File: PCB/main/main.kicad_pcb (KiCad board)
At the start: 2 copper layers, 4 parts, among them J1 Conn_01x33_Female, J2 Conn_01x33_Female, J3 Conn_01x33_Female, J4 Conn_01x33_Female

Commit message: Updated kicad_pcb file
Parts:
- added BT1: Battery, EEE3088F_Footprints:18650_Holder_THT, F.Cu at (228.6, 76.2)
- added C1: 22u, EEE3088F_Footprints:CAPC3216X180N, F.Cu at (278.9, 69.7)
- added C10: 100nF, EEE3088F_Footprints:CAPC1005X55N, F.Cu at (228.9, 109.6)
- added C11: 1.0uF, EEE3088F_Footprints:CAPC1608X90N, F.Cu at (199.6, 119.4)
- added C12: 0.1uF, EEE3088F_Footprints:CAPC1005X55N, F.Cu at (202.8, 119.2)
- added C13: 0.1uF, EEE3088F_Footprints:CAPC1005X55N, F.Cu at (213.7, 108.3)
- added C2: 10u, EEE3088F_Footprints:CAPC3216X180N, F.Cu at (270.4, 80.0)
- added C3: 22u, EEE3088F_Footprints:CAPC3216X180N, F.Cu at (222.6, 88.8)
- added C4: 10u, EEE3088F_Footprints:CAPC3216X180N, F.Cu at (203.0, 98.8)
- added C5: 0.47u, EEE3088F_Footprints:CAPC1005X55N, F.Cu at (220.2, 96.1)
- added C6: 1u, EEE3088F_Footprints:CAPC1608X90N, F.Cu at (231.0, 88.4)
- added C7: 10u, EEE3088F_Footprints:CAPC3216X180N, F.Cu at (217.4, 93.5)
- added C8: 22u, EEE3088F_Footprints:CAPC3216X180N, F.Cu at (208.2, 98.8)
- added C9: 1uF, EEE3088F_Footprints:RESC1608X55N, F.Cu at (223.3, 110.9)
- added D1: GREEN, EEE3088F_Footprints:LEDC1608X50N, F.Cu at (222.1, 93.4)
- added D2: RED, EEE3088F_Footprints:LED0805-RD_RED, F.Cu at (197.8, 98.8)
- added D3: B5819W SL, EEE3088F_Footprints:SOD-123_L2.7-W1.6-LS3.7-RD-1, F.Cu at (279.2, 66.6)
- added D4: ZMMxx, EEE3088F_Footprints:LL-34_L3.5-W1.5-RD, F.Cu at (200.6, 113.9)
- added D5: ZMMxx, EEE3088F_Footprints:LL-34_L3.5-W1.5-RD, F.Cu at (200.6, 116.8)
- added D6: ZMMxx, EEE3088F_Footprints:LL-34_L3.5-W1.5-RD, F.Cu at (210.6, 105.8)
- added D7: GREEN, EEE3088F_Footprints:LEDC1608X50N, F.Cu at (215.6, 105.9)
- added D8: GREEN, EEE3088F_Footprints:LEDC1608X50N, F.Cu at (210.1, 108.7)
- added IC1: LM358DR2G, EEE3088F_Footprints:SOIC127P600X175-8N, F.Cu at (203.2, 90.6)
- added IC2: ap2007, EEE3088F_Footprints:SOIC127P600X175-9N, F.Cu at (272.1, 68.5)
- added IC3: TP4056-42-ESOP8, EEE3088F_Footprints:SOIC127P600X175-9N, F.Cu at (272.1, 75.1)
- added IC4: LM3940IMP-3.3_NOPB, EEE3088F_Footprints:SOT230P700X180-4N, F.Cu at (194.1, 91.4)
- added IC5: CP2102-GMR, EEE3088F_Footprints:QFN50P500X500X100-29N-D, F.Cu at (204.2, 108.1)
- added J5: USB_B_Micro, EEE3088F_Footprints:MICROXNJ, F.Cu at (194.9, 105.5)
- added L1: MWSA0402S-3R3MT, EEE3088F_Footprints:INDPM4442X200N, F.Cu at (211.1, 90.3)
- added Q1: AO3401A, EEE3088F_Footprints:SOT95P280X125-3N, F.Cu at (217.4, 89.6)
- added R1: 1K2, EEE3088F_Footprints:RESC1608X55N, F.Cu at (191.4, 100.1)
- added R10: 120R, EEE3088F_Footprints:R0603, F.Cu at (216.8, 98.9)
- added R11: 1K2, EEE3088F_Footprints:RESC1608X55N, F.Cu at (205.4, 116.1)
- added R12: 4.7k, EEE3088F_Footprints:RESC2013X65N, F.Cu at (205.6, 113.3)
- added R13: 1K2, EEE3088F_Footprints:RESC1608X55N, F.Cu at (209.9, 111.4)
- added R2: 1K2, EEE3088F_Footprints:RESC1608X55N, F.Cu at (227.2, 88.5)
- added R3: 1R, EEE3088F_Footprints:R1206, F.Cu at (201.8, 95.5)
- added R4: 1R, EEE3088F_Footprints:R1206, F.Cu at (192.2, 97.2)
- added R5: 100K, EEE3088F_Footprints:RESC3116X65N, F.Cu at (207.5, 95.5)
- added R6: 33K, EEE3088F_Footprints:RESC2013X65N, F.Cu at (212.4, 94.8)
- added R7: 1K2, EEE3088F_Footprints:RESC1608X55N, F.Cu at (216.7, 96.4)
- added R8: 1K8, EEE3088F_Footprints:RESC1608X55N, F.Cu at (212.8, 98.9)
- added R9: 1K8, EEE3088F_Footprints:RESC1608X55N, F.Cu at (278.4, 72.5)
- added U1: LM61BIZ/NOPD_TempSensor(TO-92), EEE3088F_Footprints:TO-92-3_L4.9-W3.7-P1.27-L, F.Cu at (224.4, 107.5)
- added U2: LPS22HBTR_Barometer, EEE3088F_Footprints:QFN50P210X200X80-10N, F.Cu at (229.7, 106.5)
- added U3: CAT24C256, EEE3088F_Footprints:SOIC127P600X175-8N, F.Cu at (193.6, 115.8)
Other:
- board outline added: 66.7 x 19.6 mm

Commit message: Began PCB layout
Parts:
- C1, C2, C3, C4, C5, C6, C7, C8, D1, D2, D3, IC1, IC2, IC3, IC4, L1, Q1, R1, R10, R2, R3, R4, R5, R6, R7, R8, R9: moved to B.Cu
- moved IC3 163.4 mm to (111.0, 48.0), turned to -90 degrees
- moved R7 119.6 mm to (110.2, 41.8), turned to 90 degrees
- moved BT1 92.0 mm to (141.0, 48.0)
- moved C1 76.4 mm to (205.7, 48.0), turned to 180 degrees
- moved D3 76.2 mm to (206.7, 43.0), turned to 180 degrees
- moved R9 75.8 mm to (202.7, 68.0), turned to 180 degrees
- moved R1 65.6 mm to (242.5, 59.0), turned to 180 degrees
- moved IC4 58.7 mm to (237.7, 52.0), turned to 180 degrees
- moved C4 56.3 mm to (219.7, 45.0), turned to 180 degrees
- moved IC1 55.3 mm to (229.7, 42.0), turned to 180 degrees
- moved J5 55.0 mm to (242.0, 134.0)
- moved R4 54.6 mm to (232.2, 60.0), turned to 180 degrees
- moved C2 50.4 mm to (230.7, 49.0), turned to 180 degrees
- moved C8 47.7 mm to (198.7, 52.0), turned to 180 degrees
- moved Q1 46.8 mm to (212.7, 43.0), turned to 180 degrees
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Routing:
- net /Power/BAT-: track 0.00 -> 5.33 mm
- net Net-(IC3-Pad2): track 0.00 -> 2.76 mm
- added copper zone on B.Cu, net GND
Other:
- board size 66.7 x 19.6 mm -> 251.5 x 144.8 mm

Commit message: Connected voltage supply from USB to power subsystem
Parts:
- moved J5 154.5 mm to (92.2, 96.0), turned to 90 degrees
- moved R4 134.7 mm to (98.0, 48.3), turned to 90 degrees
- moved R3 116.5 mm to (94.2, 48.3), turned to 90 degrees
- moved J1 4.98 mm to (185.3, 65.5)
- moved J2 4.98 mm to (185.3, 75.6)
- moved J3 4.98 mm to (185.3, 116.2)
- moved J4 4.98 mm to (185.3, 126.4)
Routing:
- net Net-(C2-Pad1): track 0.00 -> 9.36 mm
- net GND: track 0.00 -> 1.79 mm, vias 0 -> 1

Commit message: Completed the PCB wiring
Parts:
- removed J5: USB_B_Micro, EEE3088F_Footprints:MICROXNJ
- added U4: MICROXNJ, EEE3088F_Footprints(new):MICRO-USB-SMD_MICROXNJ, B.Cu at (95.6, 97.4)
- C10, C11, C12, C13, C9, D4, D5, D6, D7, D8, IC5, R11, R12, R13, U1, U2, U3: moved to B.Cu
- D3: moved to F.Cu
- moved IC2 148.4 mm to (94.2, 69.2), turned to 90 degrees
- moved IC4 140.4 mm to (97.3, 51.1), turned to 0 degrees
- moved C5 133.8 mm to (96.0, 62.7)
- moved IC1 132.3 mm to (97.4, 43.4)
- moved U2 124.4 mm to (108.0, 80.2), turned to -90 degrees
- moved C2 124.4 mm to (106.8, 38.1)
- moved R5 123.9 mm to (95.5, 57.5), turned to -90 degrees
- moved R1 121.3 mm to (121.3, 60.2)
- moved C4 121.1 mm to (98.8, 37.5)
- moved C3 120.5 mm to (93.0, 57.5), turned to -90 degrees
- moved Q1 119.4 mm to (93.5, 37.5)
- moved R2 118.3 mm to (107.5, 60.3), turned to 0 degrees
- moved L1 116.8 mm to (94.3, 80.5), turned to 0 degrees
- moved R6 116.2 mm to (92.5, 62.5), turned to -90 degrees
- moved C1 115.5 mm to (93.6, 75.8), turned to 0 degrees
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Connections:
- C11 pad 2: /microcontroller_interfacing/BEGIN -> /USB_5V
- C13 pad 2: /microcontroller_interfacing/BEGIN -> /USB_5V
- D4 pad 1: /microcontroller_interfacing/BEGIN -> /USB_5V
- IC5 pad 7: /microcontroller_interfacing/BEGIN -> /USB_5V
- IC5 pad 8: /microcontroller_interfacing/BEGIN -> /USB_5V
- R11 pad 1: /microcontroller_interfacing/BEGIN -> /USB_5V
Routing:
- net /3V3: track 0.00 -> 125.0 mm, vias 0 -> 2
- net GND: track 1.79 -> 110.6 mm, vias 1 -> 15
- net /Power/BAT+: track 0.00 -> 98.9 mm, vias 0 -> 1
- net /USB_5V: track 0.00 -> 69.5 mm, vias 0 -> 2
- net Net-(C2-Pad1): track 9.36 -> 62.3 mm
- net /Power/V_UVLO: track 0.00 -> 46.0 mm
- net Net-(D4-Pad2): track 0.00 -> 45.4 mm
- net /microcontroller_interfacing/D-: track 0.00 -> 30.0 mm, vias 0 -> 2
- net /PA10: track 0.00 -> 27.9 mm, vias 0 -> 2
- net /PA9: track 0.00 -> 26.1 mm
- net /microcontroller_interfacing/D+: track 0.00 -> 25.7 mm
- net /PB11: track 0.00 -> 23.3 mm, vias 0 -> 2
- net Net-(D1-Pad1): track 0.00 -> 19.7 mm
- net Net-(D2-Pad1): track 0.00 -> 19.3 mm
- net /PC5: track 0.00 -> 18.2 mm
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
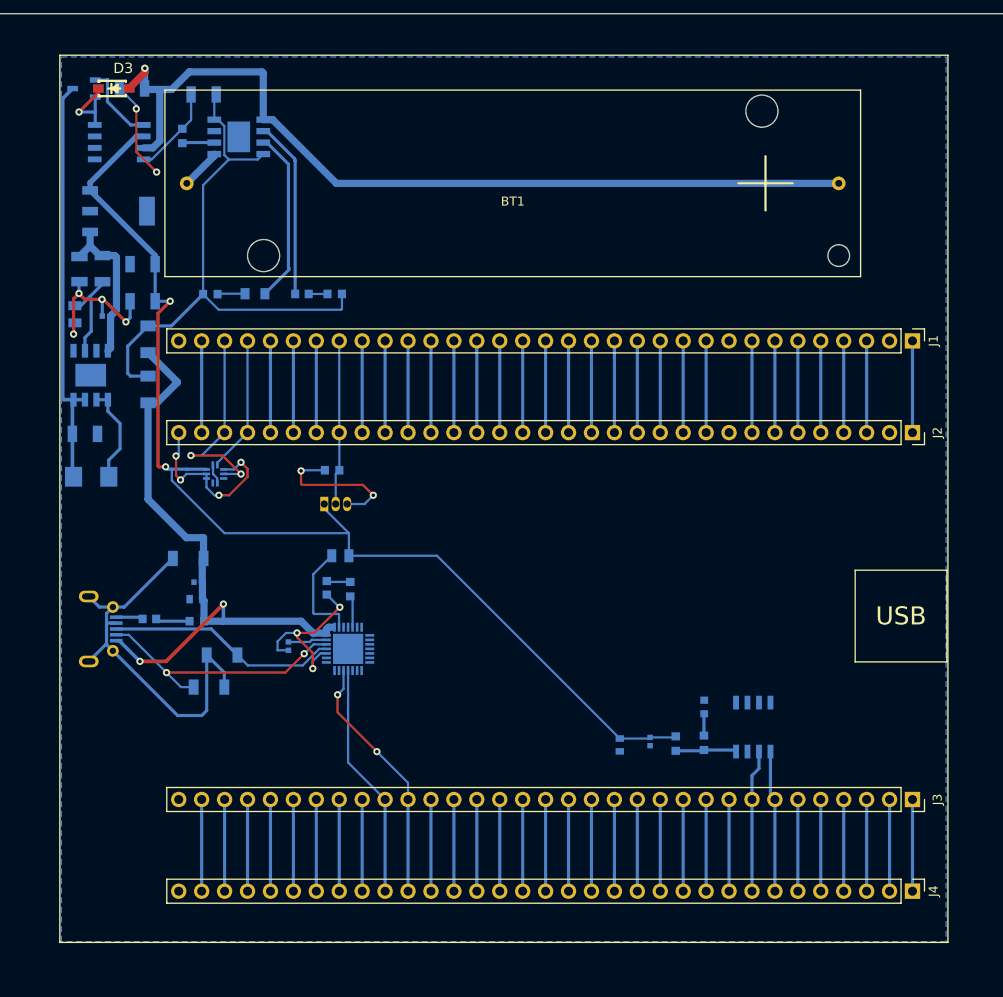
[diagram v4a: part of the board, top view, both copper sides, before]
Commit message: Fixed up some of the wiring on the PCB
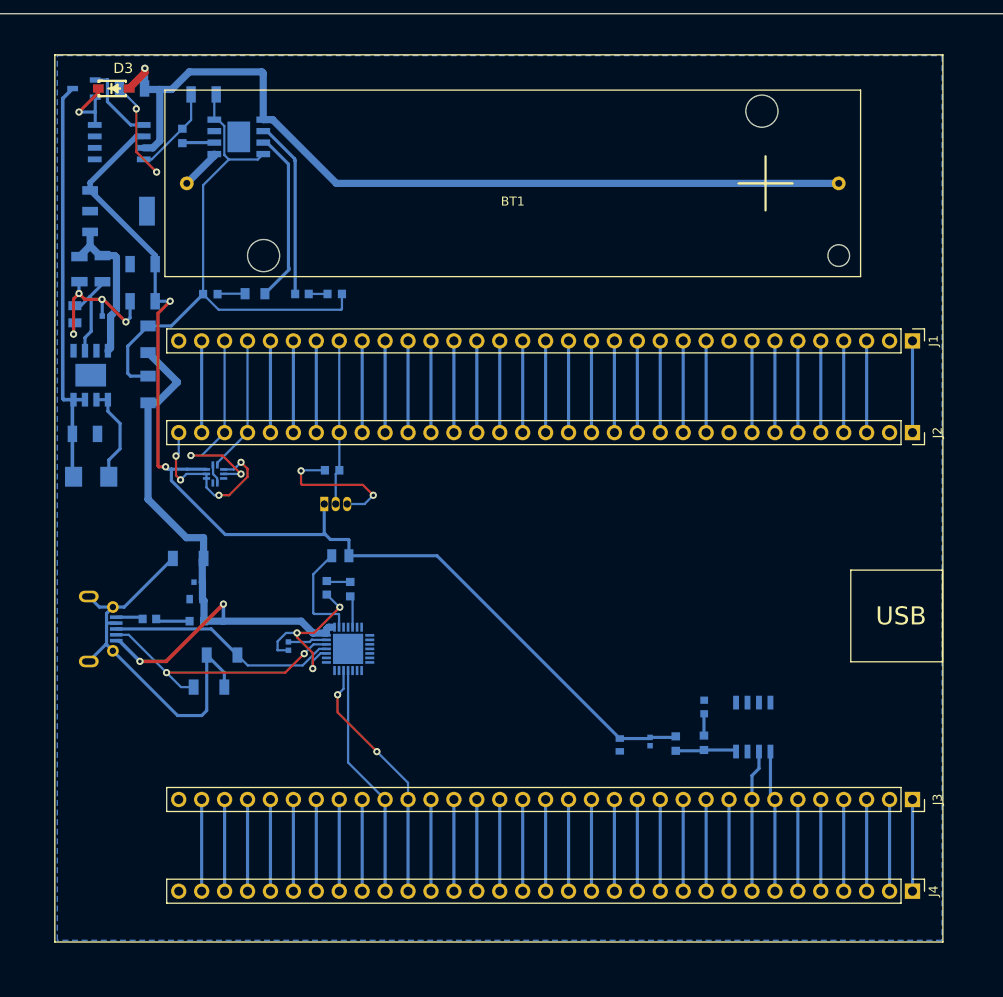
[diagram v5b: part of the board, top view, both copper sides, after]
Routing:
- net /3V3: track 125.0 -> 124.4 mm
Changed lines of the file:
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@@
       (effects (font (size 1.27 1.27) (thickness 0.254)) (justify mirror))
     )
-    (fp_text user "${REFERENCE}" (at 1.5 -2.65 180) (layer "B.Fab")
+    (fp_text user "${REFERENCE}" (at 1.5 -3.2 180) (layer "B.Fab")
       (effects (font (size 1.27 1.27) (thickness 0.254)) (justify mirror))
     )
@@
     )
   )
-  (gr_rect (start 90.8304 132.08) (end 189.2046 33.8074) (layer "B.SilkS") (width 0.15) (fill none))
-  (gr_rect (start 90.8304 33.8074) (end 189.2046 132.08) (layer "F.SilkS") (width 0.15) (fill none))
-  (gr_rect (start 178.93 90.85) (end 189.09 101.01) (layer "F.SilkS") (width 0.1) (fill none))
+  (gr_rect (start 90.2758 132.1363) (end 188.65 33.8637) (layer "B.SilkS") (width 0.15) (fill none))
+  (gr_rect (start 90.2758 33.7637) (end 188.65 132.0363) (layer "F.SilkS") (width 0.15) (fill none))
+  (gr_rect (start 178.44 90.84) (end 188.6 101) (layer "F.SilkS") (width 0.1) (fill none))
   (gr_rect (start 40.64 29.21) (end 292.1 173.99) (layer "Edge.Cuts") (width 0.1) (fill none))
-  (gr_line (start 189.09 69.26) (end 189.09 122.6) (layer "F.Fab") (width 0.1))
+  (gr_line (start 188.65 56.28) (end 188.65 109.62) (layer "F.Fab") (width 0.1))
   (gr_line (start 100.19 122.6) (end 100.19 69.26) (layer "F.Fab") (width 0.1))
-  (gr_line (start 100.19 69.26) (end 189.09 69.26) (layer "F.Fab") (width 0.1))
-  (gr_line (start 189.09 122.6) (end 100.19 122.6) (layer "F.Fab") (width 0.1))
-  (gr_rect (start 178.93 90.85) (end 189.09 101.01) (layer "F.Fab") (width 0.1) (fill none))
+  (gr_line (start 99.75 69.26) (end 188.65 69.26) (layer "F.Fab") (width 0.1))
+  (gr_line (start 188.65 122.6) (end 100.19 122.6) (layer "F.Fab") (width 0.1))
+  (gr_rect (start 178.44 90.84) (end 188.6 101) (layer "F.Fab") (width 0.1) (fill none))
   (gr_text "USB" (at 184.01 95.93) (layer "F.SilkS")
     (effects (font (size 2 2) (thickness 0.3)))
@@
   (via (at 102.55 79.4) (size 0.8) (drill 0.4) (layers "F.Cu" "B.Cu") (net 68))
   (via (at 103.05 61.05) (size 0.8) (drill 0.4) (layers "F.Cu" "B.Cu") (net 68))
-  (segment (start 156.21 109.3724) (end 158.9406 109.3724) (width 0.25) (layer "B.Cu") (net 68))
+  (segment (start 120.8 87.45) (end 122.8 87.45) (width 0.35) (layer "B.Cu") (net 68))
   (segment (start 94.1824 47.921078) (end 94.1824 48.7794) (width 0.6) (layer "B.Cu") (net 68))
-  (segment (start 156.083 109.4994) (end 156.21 109.3724) (width 0.25) (layer "B.Cu") (net 68))
-  (segment (start 132.6078 89.25) (end 152.8572 109.4994) (width 0.25) (layer "B.Cu") (net 68))
   (segment (start 94.1824 48.7794) (end 101.39 55.987) (width 0.6) (layer "B.Cu") (net 68))
-  (segment (start 122.85 89.25) (end 122.85 86.75) (width 0.25) (layer "B.Cu") (net 68))
-  (segment (start 122.85 86.75) (end 109.075386 86.75) (width 0.25) (layer "B.Cu") (net 68))
+  (segment (start 103.186711 79.663289) (end 103.186711 80.932036) (width 0.35) (layer "B.Cu") (net 68))
   (segment (start 102.55 79.4) (end 102.813289 79.663289) (width 0.35) (layer "B.Cu") (net 68))
   (segment (start 100.121 42.799) (end 99.304478 42.799) (width 0.6) (layer "B.Cu") (net 68))
   (segment (start 103.0384 61.0616) (end 103.05 61.05) (width 0.35) (layer "B.Cu") (net 68))
+  (segment (start 103.186711 80.932036) (end 109.154675 86.9) (width 0.35) (layer "B.Cu") (net 68))
   (segment (start 120.1166 84.0166) (end 120.1166 83.519491) (width 0.25) (layer "B.Cu") (net 68))
-  (segment (start 158.9406 109.3724) (end 159.0548 109.2582) (width 0.25) (layer "B.Cu") (net 68))
-  (segment (start 122.85 86.75) (end 120.1166 84.0166) (width 0.25) (layer "B.Cu") (net 68))
-  (segment (start 102.813289 79.663289) (end 103.236711 79.663289) (width 0.35) (layer "B.Cu") (net 68))
+  (segment (start 156.083 109.4994) (end 156.21 109.3724) (width 0.35) (layer "B.Cu") (net 68))
+  (segment (start 122.8 87.45) (end 122.85 87.5) (width 0.35) (layer "B.Cu") (net 68))
+  (segment (start 120.1166 86.7666) (end 120.1166 83.519491) (width 0.35) (layer "B.Cu") (net 68))
+  (segment (start 158.9406 109.3724) (end 159.0548 109.2582) (width 0.35) (layer "B.Cu") (net 68))
+  (segment (start 109.154675 86.9) (end 120.25 86.9) (width 0.35) (layer "B.Cu") (net 68))
   (segment (start 103.236711 79.663289) (end 104.936711 79.663289) (width 0.35) (layer "B.Cu") (net 68))
+  (segment (start 132.6078 89.25) (end 152.8572 109.4994) (width 0.35) (layer "B.Cu") (net 68))
+  (segment (start 102.813289 79.663289) (end 103.186711 79.663289) (width 0.35) (layer "B.Cu") (net 68))
   (segment (start 101.39 61.0616) (end 101.39 56.9468) (width 0.35) (layer "B.Cu") (net 68))
   (segment (start 101.39 61.0616) (end 103.0384 61.0616) (width 0.35) (layer "B.Cu") (net 68))
+  (segment (start 152.8572 109.4994) (end 156.083 109.4994) (width 0.35) (layer "B.Cu") (net 68))
   (segment (start 104.936711 79.663289) (end 107.0762 79.663289) (width 0.35) (layer "B.Cu") (net 68))
+  (segment (start 122.85 87.5) (end 122.85 89.25) (width 0.35) (layer "B.Cu") (net 68))
   (segment (start 99.304478 42.799) (end 94.1824 47.921078) (width 0.6) (layer "B.Cu") (net 68))
-  (segment (start 122.85 89.25) (end 132.6078 89.25) (width 0.25) (layer "B.Cu") (net 68))
-  (segment (start 103.236711 80.911325) (end 103.236711 79.663289) (width 0.25) (layer "B.Cu") (net 68))
+  (segment (start 103.186711 79.663289) (end 103.236711 79.663289) (width 0.35) (layer "B.Cu") (net 68))
+  (segment (start 120.1166 86.7666) (end 120.8 87.45) (width 0.35) (layer "B.Cu") (net 68))
+  (segment (start 156.21 109.3724) (end 158.9406 109.3724) (width 0.35) (layer "B.Cu") (net 68))
   (segment (start 101.39 55.987) (end 101.39 56.9468) (width 0.6) (layer "B.Cu") (net 68))
-  (segment (start 109.075386 86.75) (end 103.236711 80.911325) (width 0.25) (layer "B.Cu") (net 68))
-  (segment (start 152.8572 109.4994) (end 156.083 109.4994) (width 0.25) (layer "B.Cu") (net 68))
+  (segment (start 120.25 86.9) (end 120.1166 86.7666) (width 0.35) (layer "B.Cu") (net 68))
+  (segment (start 122.85 89.25) (end 132.6078 89.25) (width 0.35) (layer "B.Cu") (net 68))
   (segment (start 118.75 98.55) (end 118.768 98.568) (width 0.25) (layer "B.Cu") (net 69))
   (segment (start 116.15 98.8) (end 118.5 98.8) (width 0.25) (layer "B.Cu") (net 69))
@@
     (polygon
       (pts
-        (xy 189 132)
-        (xy 91 132)
-        (xy 91 34)
-        (xy 189 34)
+        (xy 188.55 131.85)
+        (xy 90.55 131.85)
+        (xy 90.55 33.85)
+        (xy 188.55 33.85)
       )
     )
